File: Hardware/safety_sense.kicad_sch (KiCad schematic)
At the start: 30 parts, among them U11 TLP291-4, U12 TLP291-4, U13 FODM217B

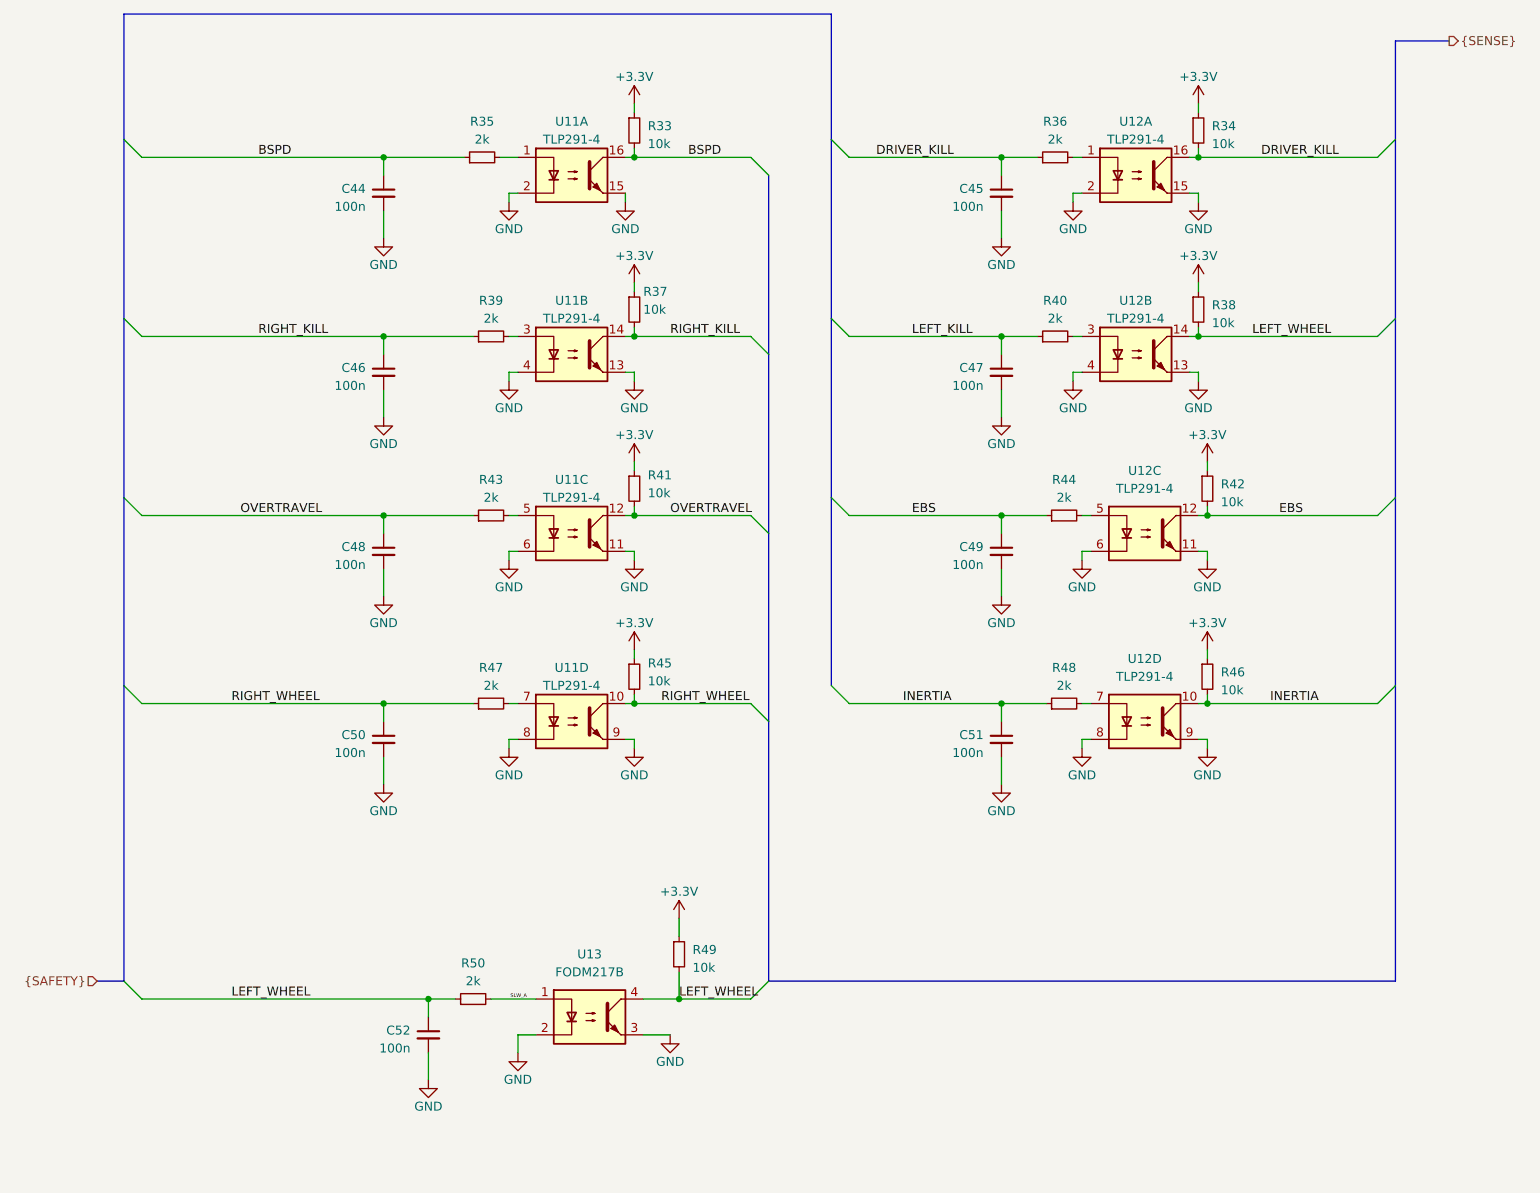
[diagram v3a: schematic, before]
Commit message: Changes in schematic, separated CAN buses, added XIAO Sense S3 DevBoard
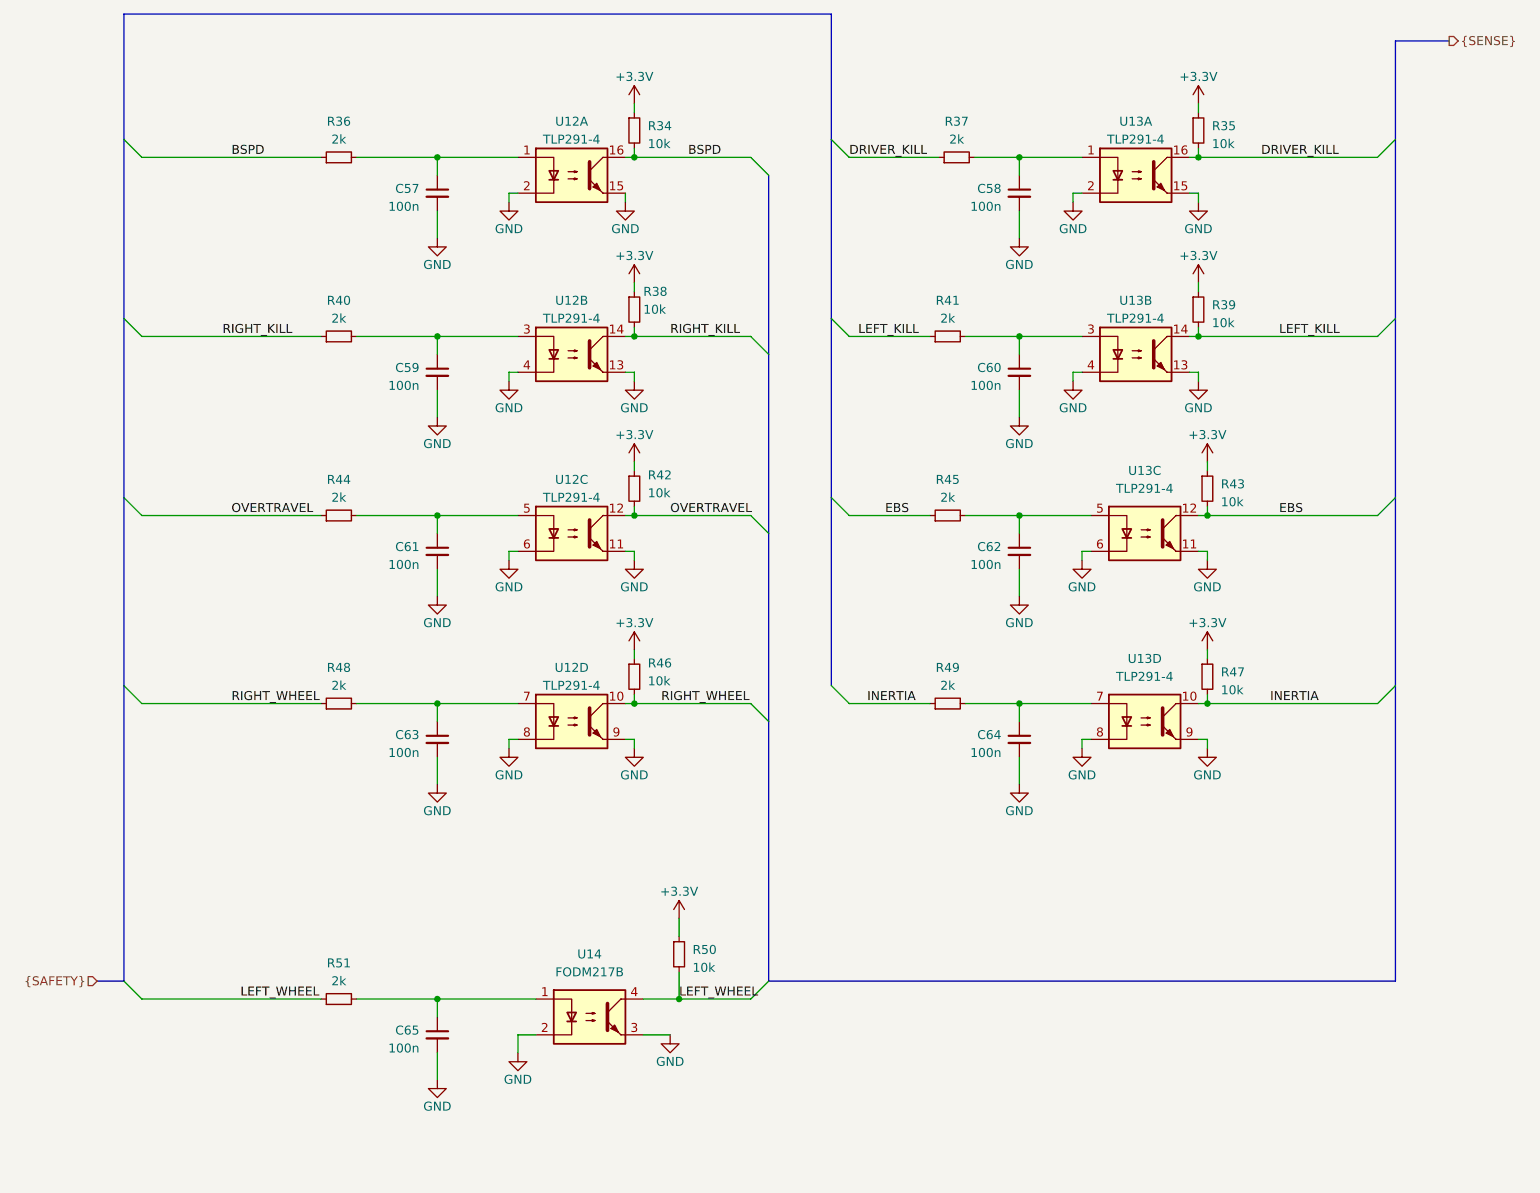
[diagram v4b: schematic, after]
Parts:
- renumbered C44 to C57, C45 to C58, C46 to C59, C47 to C60, C48 to C61, C49 to C62, C50 to C63, C51 to C64, C52 to C65, R33 to R34, R34 to R35, R35 to R36, R36 to R37, R37 to R38, R38 to R39, R39 to R40, R40 to R41, R41 to R42, R42 to R43, R43 to R44, R44 to R45, R45 to R46, R46 to R47, R47 to R48, R48 to R49, R49 to R50, R50 to R51, U11 to U12, U12 to U13, U13 to U14
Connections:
- net BSPD: no longer C57.1
- net DRIVER_KILL: no longer C58.1
- net EBS: no longer C62.1
- net INERTIA: no longer C64.1
- net LEFT_KILL: now also R39.2, U13.14; no longer C60.1
- net LEFT_WHEEL: no longer C65.1, R39.2, U13.14
- net OVERTRAVEL: no longer C61.1
- net RIGHT_KILL: no longer C59.1
- net RIGHT_WHEEL: no longer C63.1
- net at R41.2, U13.3: now also C60.1
- net at R40.2, U12.3: now also C59.1
- net at R45.2, U13.5: now also C62.1
- net at R36.2, U12.1: now also C57.1
- net at R48.2, U12.7: now also C63.1
- net at R49.2, U13.7: now also C64.1
- net at R44.2, U12.5: now also C61.1
- net at R37.2, U13.1: now also C58.1
- net SLW_A: no longer names the net of R51.2, U14.1
- net SLW_A: now also C65.1
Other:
- moved on the sheet: C57, C58, C59, C60, C61, C62, C63, C64, C65, R36, R37, R40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

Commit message: Initial layout, changes in safety sensing bus labels
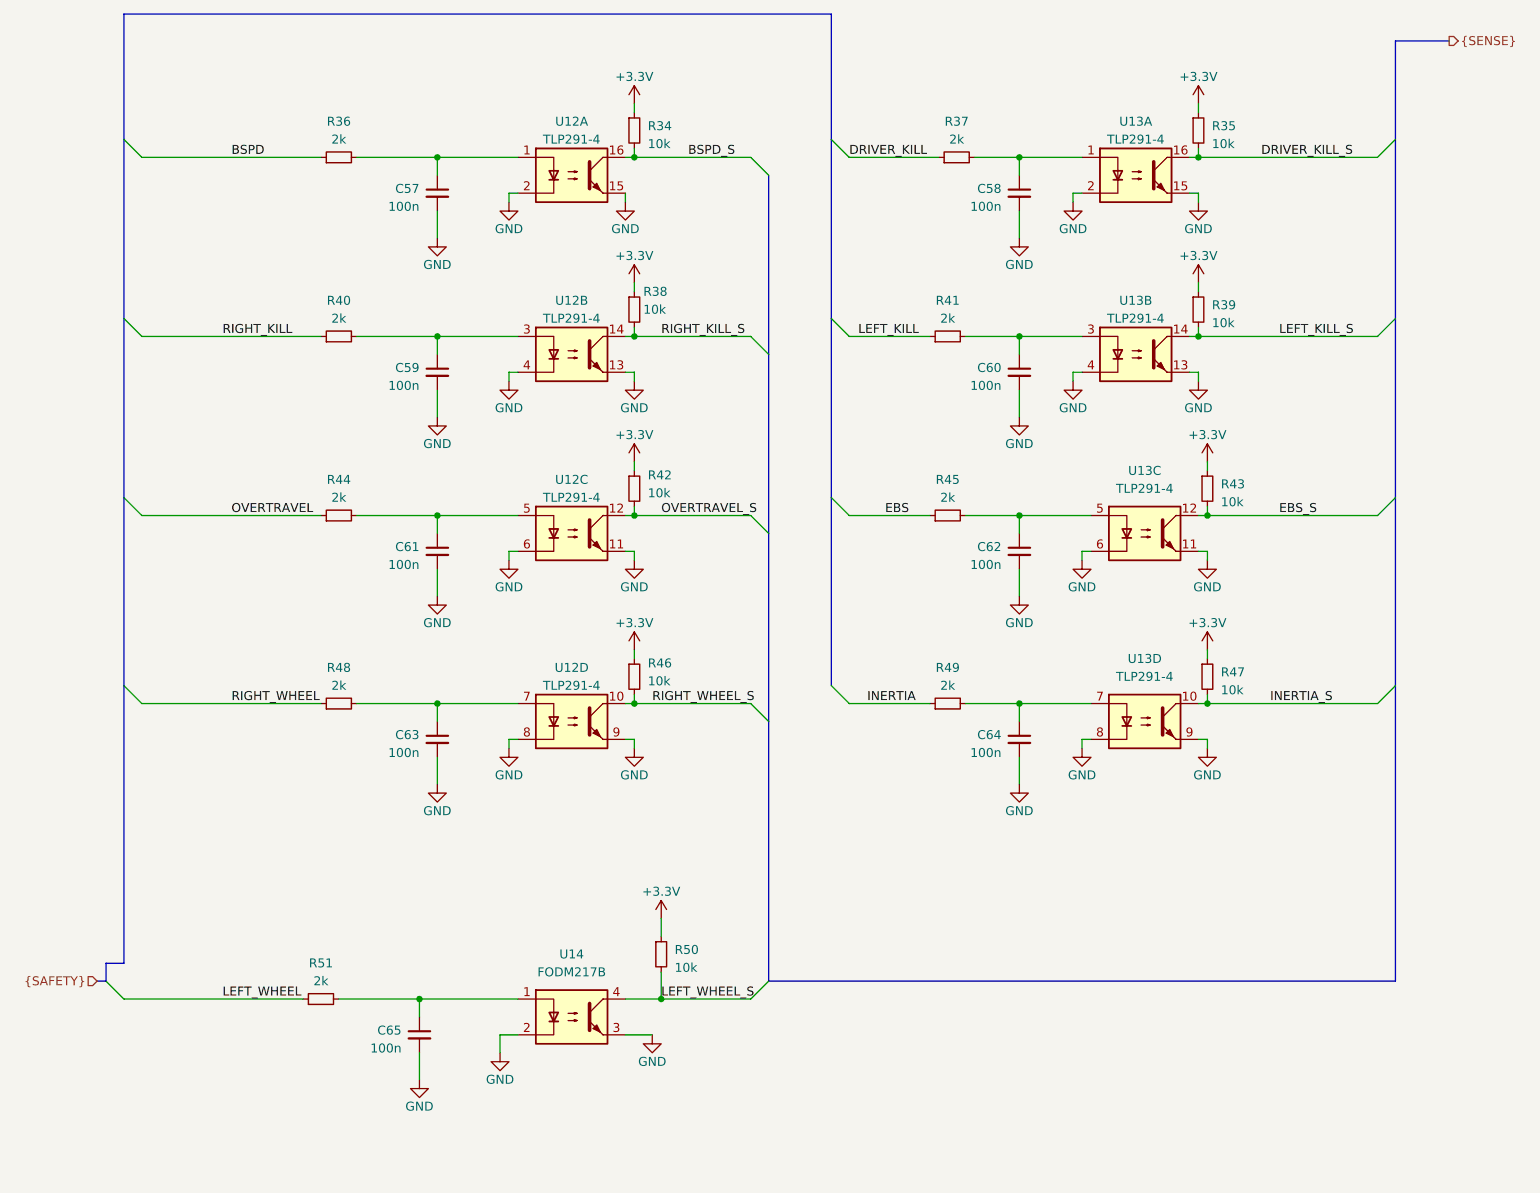
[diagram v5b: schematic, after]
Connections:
- net BSPD: no longer R34.2, U12.16
- net DRIVER_KILL: no longer R35.2, U13.16
- net EBS: no longer R43.2, U13.12
- net INERTIA: no longer R47.2, U13.10
- net LEFT_KILL: no longer R39.2, U13.14
- net LEFT_WHEEL: no longer R50.2, U14.4
- net OVERTRAVEL: no longer R42.2, U12.12
- net RIGHT_KILL: no longer R38.2, U12.14
- net RIGHT_WHEEL: no longer R46.2, U12.10
- new net BSPD_S: R34.2, U12.16
- new net DRIVER_KILL_S: R35.2, U13.16
- new net EBS_S: R43.2, U13.12
- new net INERTIA_S: R47.2, U13.10
- new net LEFT_KILL_S: R39.2, U13.14
- new net LEFT_WHEEL_S: R50.2, U14.4
- new net OVERTRAVEL_S: R42.2, U12.12
- new net RIGHT_KILL_S: R38.2, U12.14
- new net RIGHT_WHEEL_S: R46.2, U12.10
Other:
- moved on the sheet: C65, R50, R51, U14

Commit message: Changes in CAN section
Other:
- title: (none) -> FrontBox
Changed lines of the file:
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@@
 	(generator_version "9.0")
 	(paper "A4")
+	(title_block
+		(title "FrontBox")
+	)
 	(bus_alias "SENSE"
 		(members "BSPD_S" "RIGHT_KILL_S" "OVERTRAVEL_S" "RIGHT_WHEEL_S" "LEFT_WHEEL_S"

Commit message: BOM update
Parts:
- C57, C58, C59, C60, C61, C62, C63, C64, C65, R34, R35, R36, R37, R38, R39, R40, R41, R42, R43, R44, R45, R46, R47, R48, R49, R50, R51: Mouser Part Number (none) -> .
- U12, U13: Mouser Part Number (none) -> 757-TLP293-4TPRE
- U14: Mouser Part Number (none) -> 512-FODM217B
